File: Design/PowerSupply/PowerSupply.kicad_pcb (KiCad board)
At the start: 2 copper layers, 35 x 32 mm, 16 parts, among them J1 Barrel_Jack, J2 Conn_01x02_Male, Q1 IRF644, U1 MAX1771

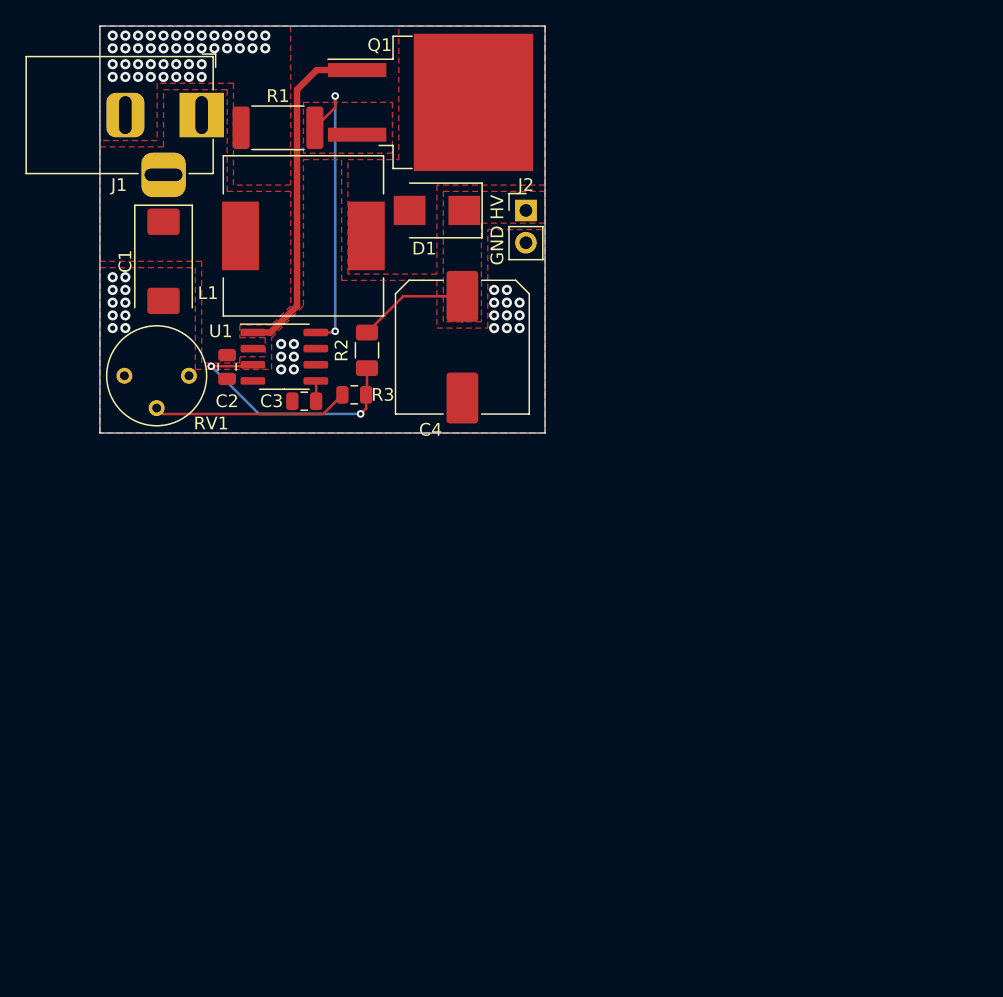
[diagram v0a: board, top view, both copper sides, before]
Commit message: Add license notice to all human readable files
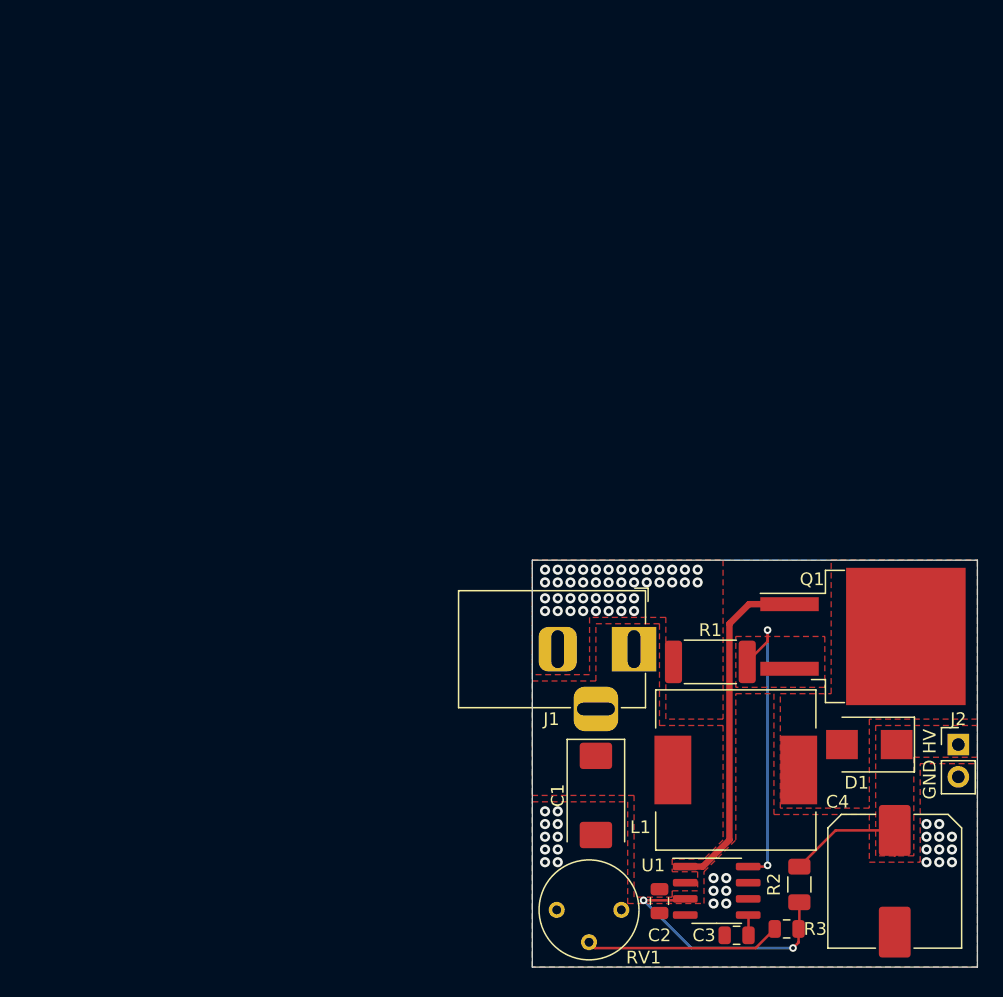
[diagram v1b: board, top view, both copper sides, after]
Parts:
- moved C1 54.0 mm to (135.0, 90.5)
- moved C2 54.0 mm to (140.0, 98.8)
- moved C3 54.0 mm to (146.1, 101.5)
- moved C4 54.0 mm to (158.5, 97.2)
- moved CAUTION 54.0 mm to (157.2, 87.8)
- moved D1 54.0 mm to (156.5, 86.5)
- moved J1 54.0 mm to (138.0, 79.0)
- moved J2 54.0 mm to (163.5, 86.5)
- moved L1 54.0 mm to (146.0, 88.5)
- moved Q1 54.0 mm to (156.0, 78.0)
- moved R1 54.0 mm to (144.0, 80.0)
- moved R2 54.0 mm to (151.0, 97.5)
- moved R3 54.0 mm to (150.0, 101.0)
- moved REF** 54.0 mm to (148.5, 78.0)
- moved RV1 54.0 mm to (137.0, 99.5)
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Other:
- board text added: "Nixie Power Supply PCB Copyright (C) 2020 Daniel He See <https://www.gnu.org/licenses/>."
- board text added: "Nixie Power Supply PCB Copyright (C) 2020 Daniel He This program is free software: you can redistribute it and/or modify it under the terms of the GNU General Public License as published by the Free Software Foundation, either version 3 of the License, or (at your option) any later version. This program is distributed in the hope that it will be useful, but WITHOUT ANY WARRANTY; without even the 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"
